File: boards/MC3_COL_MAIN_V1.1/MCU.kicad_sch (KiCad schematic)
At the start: 52 parts, among them J2 SWD, SW1 SKRKAEE020, U10 GP1S094HCZ0F, U11 GP1S094HCZ0F, U2 STM32U595RJT6, U9 AEDR-8300-1Q0, Y1 8MHz

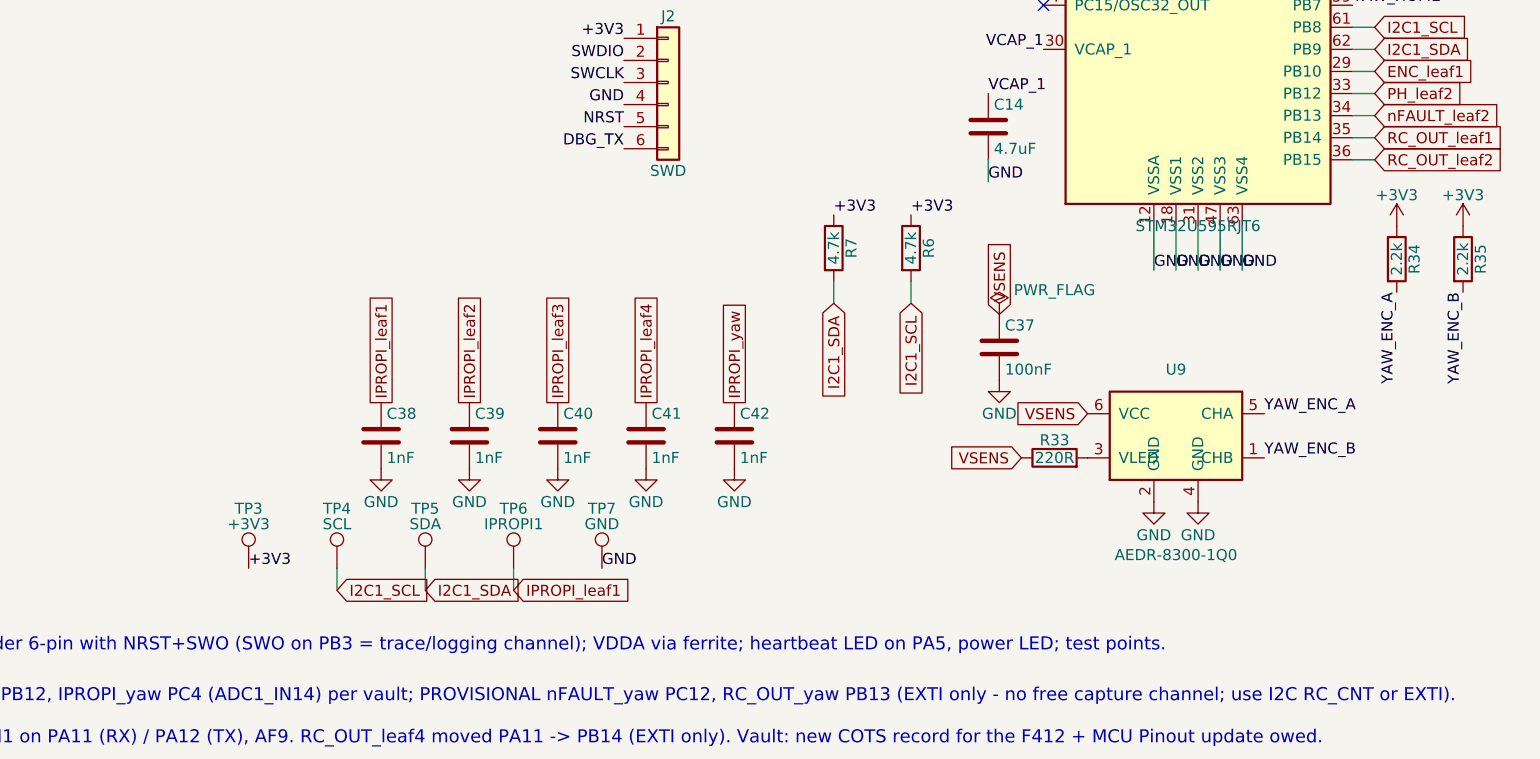
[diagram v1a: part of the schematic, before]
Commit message: Vault consolidation: Main-Board-02 rung folded back into Main-Board-01
Nothing was built at V1.0, so the 24 V revision never justified a rung bump.
Main-Board-01 now builds boards/MC3_COL_MAIN_V1.1 (24 V input); V1.0 stays in
the repo as the 5 V-only fallback revision. Repo side: CLAUDE.md rung mapping,
MIGRATION.md header and §14 pointer, LM61460 layout-note link. Vault side
(edited directly): Main-Board-01 Power rewritten as the 24 V chain, rung page
carries the V1.0→V1.1 delta/BOM/gates, Main-Board-02 folder deleted, 13 pages'
references rewritten.

Co-Authored-By: Claude Fable 5 <noreply@anthropic.com>
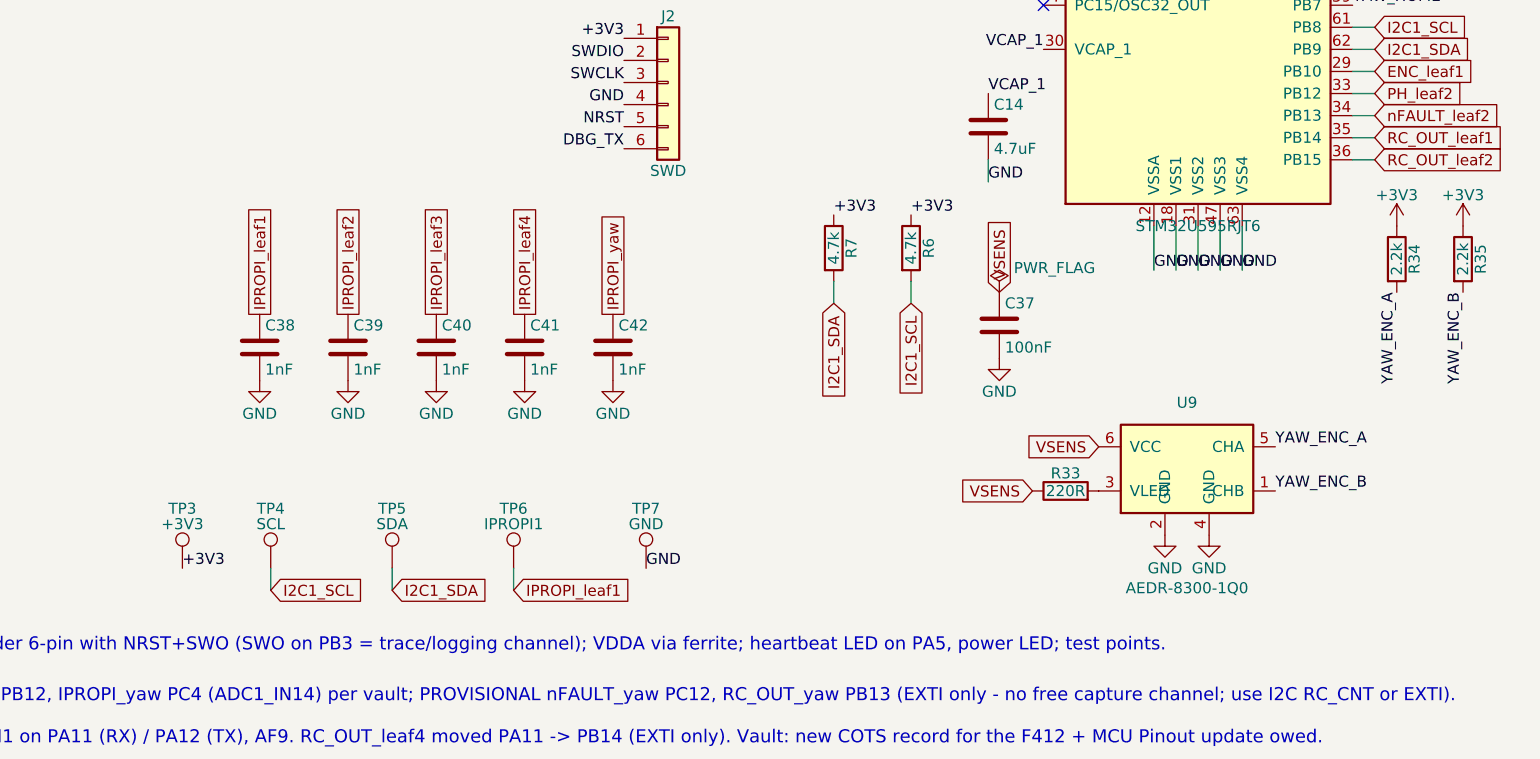
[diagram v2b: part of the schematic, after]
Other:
- moved on the sheet: C37, C38, C39, C40, C41, C42, R33, TP3, TP4, TP5, TP7, U9

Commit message: V1.1 schematics: per-instance Description fields on ~63 symbols
The component-docs Role source of record. Netlist unchanged, ERC 0.

Co-Authored-By: Claude Fable 5 <noreply@anthropic.com>
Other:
- note removed: "2026-08-22: MCU is now STM32F412RET6 (pin-identical to the F411RET6; adds bxCAN x2 and 256 KB RAM). CAN1 on PA11 (RX) / PA12 (TX), AF9. RC_OUT_leaf4 moved PA11 -> PB14 (EXTI only). Vault: new COTS record for the F412 + MCU Pinout update owed."
- note removed: "2026-08-22: yaw channel FITTED (user decision, supersedes the 'reserved only' note above): EN_yaw PA9 (TIM1_CH2), PH_yaw PB12, IPROPI_yaw PC4 (ADC1_IN14) per vault; PROVISIONAL nFAULT_yaw PC12, RC_OUT_yaw PB13 (EXTI only - no free capture channel; use I2C RC_CNT or EXTI)."
- note removed: "MCU - STM32F411RET6 LQFP64. Implements: COL-COTS-0024. Pin map: vault Main-Board-01 MCU Pinout (EN on TIM3, IPROPI on ADC1 E/S edges, ENC on TIM2/TIM1 capture). Layout: docs/design/parts/STM32F411.md. Yaw reserved pins PA9/PB12/PC4 left unconnected per vault. PROVISIONAL (owed to vault): I2C1 on PB8/PB9, DRV_nSLEEP on PC5, nFAULT on PC0-2/PC10, RC_OUT on PB6/PB7/PA10/PA11."
- note removed: "Review 2026-08-22: HSE caps 33pF (crystal CL=20pF); NRST 100nF; SWD header 6-pin with NRST+SWO (SWO on PB3 = trace/logging channel); VDDA via ferrite; heartbeat LED on PA5, power LED; test points."
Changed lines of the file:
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@@
 	(generator_version "10.0")
 	(paper "A4")
-	(text "2026-08-22: yaw channel FITTED (user decision, supersedes the 'reserved only' note above): EN_yaw PA9 (TIM1_CH2), PH_yaw PB12, IPROPI_yaw PC4 (ADC1_IN14) per vault; PROVISIONAL nFAULT_yaw PC12, RC_OUT_yaw PB13 (EXTI only - no free capture channel; use I2C RC_CNT or EXTI)."
-		(exclude_from_sim no)
-		(at 29.972 200.152 0)
-		(effects
-			(font
-				(size 1.5 1.5)
-			)
-		)
-	)
-	(text "Review 2026-08-22: HSE caps 33pF (crystal CL=20pF); NRST 100nF; SWD header 6-pin with NRST+SWO (SWO on PB3 = trace/logging channel); VDDA via ferrite; heartbeat LED on PA5, power LED; test points."
-		(exclude_from_sim no)
-		(at 38.354 194.31 0)
-		(effects
-			(font
-				(size 1.5 1.5)
-			)
-		)
-	)
-	(text "MCU - STM32F411RET6 LQFP64. Implements: COL-COTS-0024. Pin map: vault Main-Board-01 MCU Pinout (EN on TIM3, IPROPI on ADC1 E/S edges, ENC on TIM2/TIM1 capture). Layout: docs/design/parts/STM32F411.md. Yaw reserved pins PA9/PB12/PC4 left unconnected per vault. PROVISIONAL (owed to vault): I2C1 on PB8/PB9, DRV_nSLEEP on PC5, nFAULT on PC0-2/PC10, RC_OUT on PB6/PB7/PA10/PA11."
-		(exclude_from_sim no)
-		(at 99.06 212.852 0)
-		(effects
-			(font
-				(size 1.5 1.5)
-			)
-		)
-	)
-	(text "2026-08-22: MCU is now STM32F412RET6 (pin-identical to the F411RET6; adds bxCAN x2 and 256 KB RAM). CAN1 on PA11 (RX) / PA12 (TX), AF9. RC_OUT_leaf4 moved PA11 -> PB14 (EXTI only). Vault: new COTS record for the F412 + MCU Pinout update owed."
-		(exclude_from_sim no)
-		(at 30 205 0)
-		(effects
-			(font
-				(size 1.5 1.5)
-			)
-		)
-	)
 	(junction
 		(at 259.08 74.93)
@@
 			)
 		)
-		(property "Description" ""
+		(property "Description" "Addressable status pixel 1 of 2 ([[COL-COTS-0036]] XL-1010RGBC), on VM, underside; data from PB5/SPI1_MOSI."
 			(at 259.08 63.5 0)
 			(show_name no)
@@
 			)
 		)
-		(property "Description" ""
+		(property "Description" "8 MHz HSE crystal X32258MSB4SI (CL = 20 pF, 33 pF load caps)."
 			(at 90.17 100.33 0)
 			(show_name no)
@@
 			)
 		)
-		(property "Description" ""
+		(property "Description" "AEDR-8300 LED current set (~15 mA from VSENS)."
 			(at 134.62 176.53 0)
 			(show_name no)
@@
 			)
 		)
-		(property "Description" ""
+		(property "Description" "VDDA feed bead (600 Ω @ 100 MHz) — analog supply isolation for the ADC."
 			(at 137.16 38.1 0)
 			(show_name no)
@@
 			)
 		)
-		(property "Description" ""
+		(property "Description" "Heartbeat LED (green, PA5), underside."
 			(at 218.44 43.18 0)
 			(show_name no)
@@
 			)
 		)
-		(property "Description" ""
+		(property "Description" "Yaw incremental encoder [[COL-COTS-0032]] AEDR-8300, underside, reading the M10899 ring; A/B to TIM2."
 			(at 148.59 173.99 0)
 			(show_name no)
@@
 			)
 		)
-		(property "Description" ""
+		(property "Description" "Yaw far-limit interrupter [[COL-COTS-0034]] GP1S094, 180° from U10, YAW_LIM EXTI."
 			(at 217.17 129.54 0)
 			(show_name no)
@@
 			)
 		)
-		(property "Description" ""
+		(property "Description" "SWD header 1×6, underside bring-up fixture (DNP-class); pin 6 carries DBG_TX."
 			(at 88.9 129.54 0)
 			(show_name no)
@@
 			)
 		)
-		(property "Description" ""
+		(property "Description" "Power LED (red, on +3V3), underside."
 			(at 218.44 52.07 0)
 			(show_name no)
@@
 			)
 		)
-		(property "Description" ""
+		(property "Description" "Pixel data series resistor (470R) at the MCU end of the D5–D6 chain."
 			(at 241.3 63.5 0)
 			(show_name no)
@@
 			)
 		)
-		(property "Description" ""
+		(property "Description" "Yaw homing interrupter [[COL-COTS-0034]] GP1S094 — flag present = YAW_HOME high; hand-solder only, GND pins straddle the mounting post."
 			(at 217.17 105.41 0)
 			(show_name no)
@@
 			)
 		)
-		(property "Description" ""
+		(property "Description" "MCU reset button, underside."
 			(at 85.09 68.58 0)
 			(show_name no)
@@
 			)
 		)
-		(property "Description" ""
+		(property "Description" "The MCU — [[COL-COTS-0035]] STM32U595RJT6 (order the non-Q variant). Pin assignment owned by [[Main-Board-01 MCU Pinout]]."
 			(at 149.86 100.33 0)
 			(show_name no)
@@
 			)
 		)
-		(property "Description" ""
+		(property "Description" "Addressable status pixel 2 of 2 ([[COL-COTS-0036]]), chained from D5."
 			(at 259.08 91.44 0)
 			(show_name no)

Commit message: Assembly flags: U10/U11/J2 marked hand-solder, excluded from turnkey
Assembly field on the symbols (self-documenting; component pages render it);
fab-output pass will translate it to PCBWay's do-not-assemble column and drop
the three from the PnP. Netlist unchanged.

Co-Authored-By: Claude Fable 5 <noreply@anthropic.com>
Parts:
- J2, U10, U11: Assembly (none) -> hand-solder by us — exclude from turnkey assembly and PnP (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
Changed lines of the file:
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@@
 			)
 		)
-	)
+		(property "Assembly" "hand-solder by us — exclude from turnkey assembly and PnP (Sharp: no reflow)"
+			(at 217.17 129.54 0)
+			(hide yes)
+			(effects
+				(font
+					(size 1.27 1.27)
+				)
+			)
+		))
 	(symbol
 		(lib_id "power:GND")
@@
 			)
 		)
-	)
+		(property "Assembly" "hand-solder by us — exclude from turnkey assembly and PnP (bring-up fixture)"
+			(at 88.9 129.54 0)
+			(hide yes)
+			(effects
+				(font
+					(size 1.27 1.27)
+				)
+			)
+		))
 	(symbol
 		(lib_id "Device:LED")
@@
 			)
 		)
-	)
+		(property "Assembly" "hand-solder by us — exclude from turnkey assembly and PnP (Sharp: no reflow)"
+			(at 217.17 105.41 0)
+			(hide yes)
+			(effects
+				(font
+					(size 1.27 1.27)
+				)
+			)
+		))
 	(symbol
 		(lib_id "Switch:SW_Push")
